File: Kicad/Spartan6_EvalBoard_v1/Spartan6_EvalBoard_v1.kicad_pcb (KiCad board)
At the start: 4 copper layers, 50 x 37.5 mm, 98 parts, among them J201 CON2X45, P301 PWR, P401 CONN_3X2, Q301 MOSFET_N, Q301 NPN, Q401 XC6SLX16, U301 XR21B1411, U401 24LC64T, U402 MX25L8006E, X301 USBMICRO, X401 XOSC

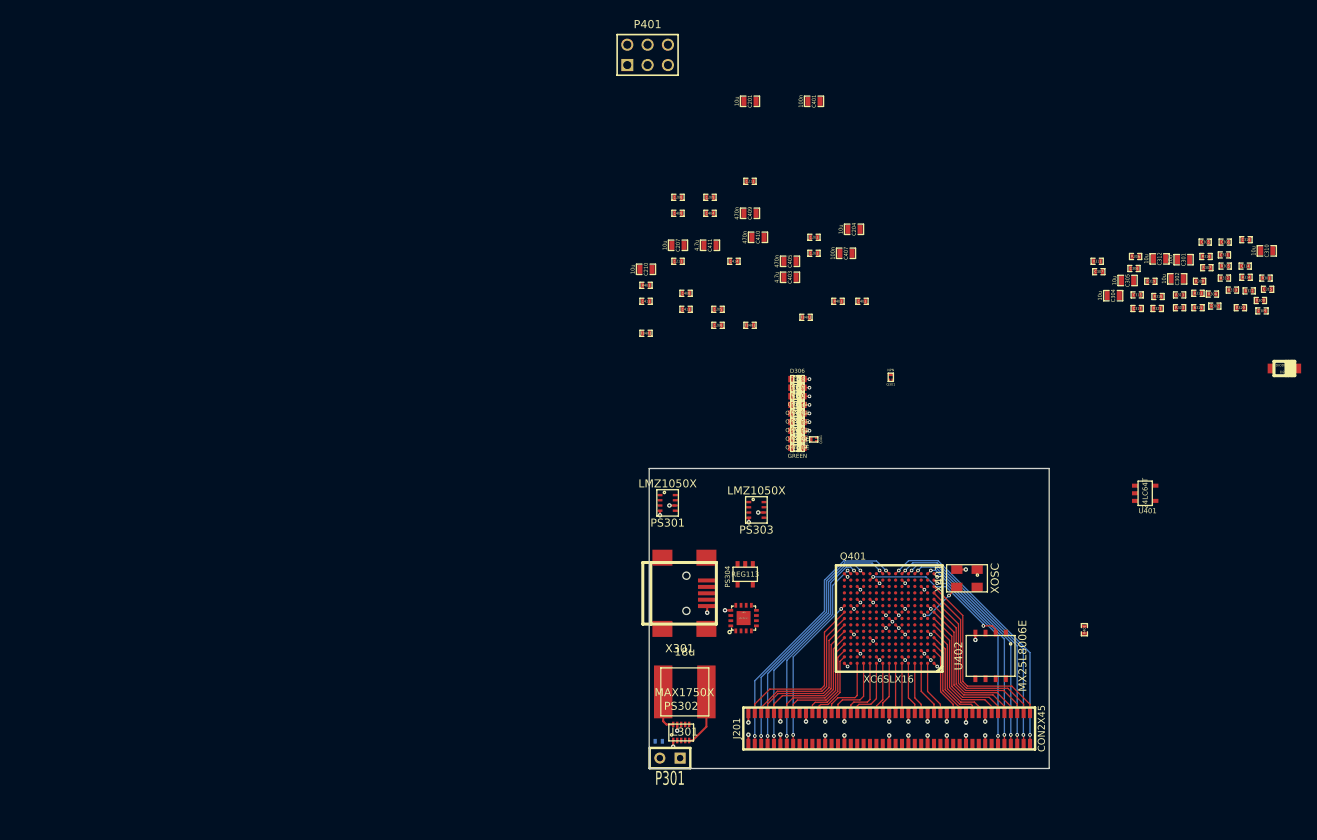
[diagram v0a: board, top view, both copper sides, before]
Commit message: BZR - Layout half done
Using LaunchPad Kicad
Layout more than half completed
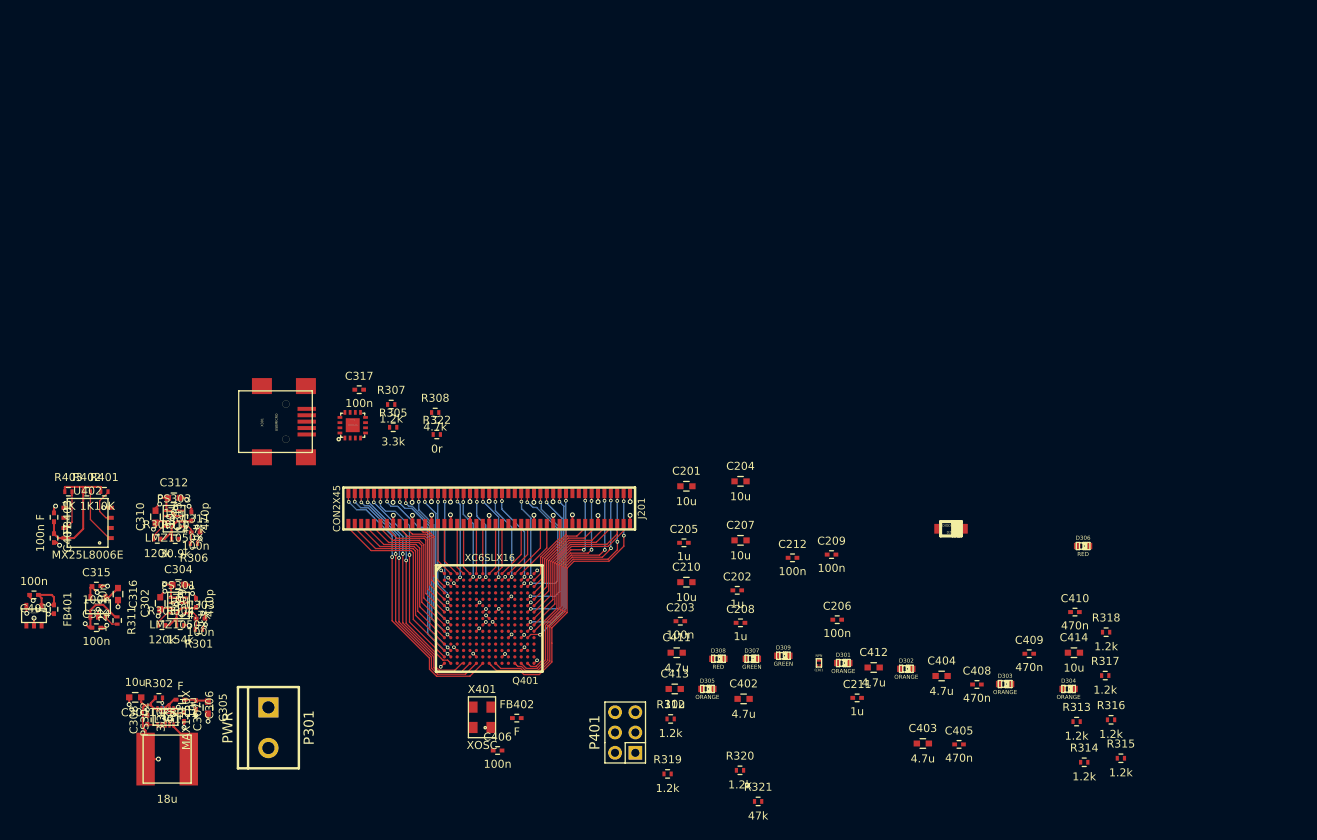
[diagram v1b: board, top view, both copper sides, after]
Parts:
- removed the Q301 at (130.2, 88.6)
- removed the Q301 at (120.6, 96.4)
- added Q301: NPN, Eric.mod:TSLP-3-1, F.Cu at (121.2, 124.3)
- C201, C204, C207, C210, C301, C302, C304, C305, C310, C312, C403, C411: footprint SM0603_Capa -> Capacitors_SMD.pretty:C_0603
- C202, C203, C205, C206, C208, C209, C211, C212, C303, C306, C307, C308, C309, C311, C313, C314, C315, C317, C406, C408: footprint SM0402_c -> Capacitors_SMD.pretty:C_0402
- C316, C402, C404, C412, C413, C414: footprint SM0402_c -> Capacitors_SMD.pretty:C_0603
- C401, C405, C407, C409, C410: footprint SM0603_Capa -> Capacitors_SMD.pretty:C_0402
- D201: footprint SOD-123FL -> Eric.mod:SOD-123FL
- D301, D302, D303, D304, D305, D306, D307, D308, D309: footprint LED-0603 -> LEDs.pretty:LED-0603
- FB301: footprint SM0402 -> Capacitors_SMD.pretty:C_0402; moved to F.Cu
- FB401, FB402, FB403: footprint SM0402 -> Capacitors_SMD.pretty:C_0402
- J201: footprint CON45X2 -> Eric.mod:CON45X2
- L301: footprint IND6x6 -> Eric.mod:IND6x6
- P301: footprint SIL-2 -> Connect.pretty:bornier2
- P401: footprint pin_array_3x2 -> Pin_Headers.pretty:Pin_Header_Straight_2x03
- PS301, PS303: footprint SIL08 -> Eric.mod:SIL08
- PS302: footprint TDFN10 -> Eric.mod:TDFN10
- PS304, U401: footprint SOT23-5 -> tinkerforge.mod:SOT23-5
- Q401: footprint CSG225 -> Eric.mod:CSG225
- R301, R302, R303, R304, R305, R306, R307, R308, R309, R310, R311, R312, R313, R314, R315, R316, R317, R318, R319, R320, R321, R322, R401, R402, R403: footprint SM0402_r -> Resistors_SMD.pretty:R_0402
- U301: footprint QFN-16 -> Eric.mod:QFN-16
- U402: footprint WSON8 -> Eric.mod:WSON8
- X301: footprint USB_MINI_B -> tinkerforge.mod:USB-MINI-B-SMD
- X401: footprint XTAL5032 -> Eric.mod:XTAL5032
- moved C315 151.0 mm to (30.9, 114.7)
- moved C314 150.5 mm to (30.9, 119.9)
- moved C316 147.8 mm to (33.6, 115.7), turned to 270 degrees
- moved C308 147.4 mm to (37.3, 131.4), turned to 90 degrees
- moved C310 142.8 mm to (38.3, 106.0), turned to 90 degrees
- moved C301 142.0 mm to (35.8, 128.6), turned to 180 degrees
- moved R302 140.8 mm to (38.7, 128.7)
- moved R301 140.4 mm to (43.7, 120.1), turned to 180 degrees
- moved U401 139.7 mm to (23.1, 118.4), turned to 0 degrees
- moved C309 138.2 mm to (43.3, 116.8), turned to 90 degrees
- moved R310 135.8 mm to (40.7, 108.8)
- moved R304 135.5 mm to (41.4, 119.6)
- moved R309 134.2 mm to (38.5, 108.8)
- moved C303 134.1 mm to (43.9, 118.8)
- moved C302 133.4 mm to (38.9, 116.8), turned to 90 degrees
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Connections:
- J201 pad 14: (no net) -> /IO Connector/IO14
- J201 pad 18: (no net) -> /IO Connector/IO18
- J201 pad 20: (no net) -> /IO Connector/IO20
- J201 pad 24: (no net) -> /IO Connector/IO24
- J201 pad 26: (no net) -> /IO Connector/IO26
- J201 pad 30: (no net) -> /IO Connector/IO30
- J201 pad 32: (no net) -> /IO Connector/IO32
- J201 pad 36: (no net) -> /IO Connector/IO36
- J201 pad 38: (no net) -> /IO Connector/IO38
- J201 pad 42: (no net) -> /IO Connector/IO42
- J201 pad 44: (no net) -> /IO Connector/IO44
- J201 pad 48: (no net) -> /IO Connector/IO48
- J201 pad 50: (no net) -> /IO Connector/IO50
- J201 pad 56: (no net) -> /IO Connector/IO56
- J201 pad 58: (no net) -> /IO Connector/IO58
- J201 pad 62: (no net) -> /IO Connector/IO62
- J201 pad 64: (no net) -> /IO Connector/IO64
- J201 pad 68: (no net) -> /IO Connector/IO68
- J201 pad 70: (no net) -> /IO Connector/IO70
- PS302 pad 7: (no net) -> Net-(PS302-Pad7)
- Q401 pad B11: (no net) -> /IO Connector/IO48
- Q401 pad B13: (no net) -> /IO Connector/IO50
- Q401 pad B14: (no net) -> /IO Connector/IO56
- Q401 pad B3: (no net) -> /IO Connector/IO36
- Q401 pad B5: (no net) -> /IO Connector/IO38
- Q401 pad B7: (no net) -> /IO Connector/IO42
- Q401 pad B9: (no net) -> /IO Connector/IO44
- Q401 pad C10: (no net) -> Net-(Q401-PadC10)
- Q401 pad C11: (no net) -> Net-(Q401-PadC11)
- Q401 pad C12: (no net) -> Net-(Q401-PadC12)
- Q401 pad C14: (no net) -> /IO Connector/IO58
- Q401 pad C2: (no net) -> /IO Connector/IO32
- Q401 pad C4: (no net) -> Net-(Q401-PadC4)
- Q401 pad C5: (no net) -> Net-(Q401-PadC5)
- Q401 pad C6: (no net) -> Net-(Q401-PadC6)
- Q401 pad C7: (no net) -> Net-(Q401-PadC7)
- Q401 pad C8: (no net) -> Net-(Q401-PadC8)
- Q401 pad C9: (no net) -> Net-(Q401-PadC9)
- Q401 pad D10: (no net) -> Net-(Q401-PadD10)
- Q401 pad D11: (no net) -> Net-(Q401-PadD11)
- Q401 pad D13: (no net) -> Net-(Q401-PadD13)
- Q401 pad D3: (no net) -> Net-(Q401-PadD3)
- Q401 pad D4: (no net) -> Net-(Q401-PadD4)
- Q401 pad D5: (no net) -> Net-(Q401-PadD5)
- Q401 pad D6: (no net) -> Net-(Q401-PadD6)
- Q401 pad D7: (no net) -> Net-(Q401-PadD7)
- Q401 pad D8: (no net) -> Net-(Q401-PadD8)
- Q401 pad E14: (no net) -> /IO Connector/IO62
- Q401 pad E2: (no net) -> /IO Connector/IO30
- Q401 pad E3: (no net) -> Net-(Q401-PadE3)
- Q401 pad E4: (no net) -> Net-(Q401-PadE4)
- Q401 pad E5: (no net) -> Net-(Q401-PadE5)
- Q401 pad E6: (no net) -> Net-(Q401-PadE6)
- Q401 pad E7: (no net) -> Net-(Q401-PadE7)
- Q401 pad E8: (no net) -> Net-(Q401-PadE8)
- Q401 pad E9: (no net) -> Net-(Q401-PadE9)
- Q401 pad F10: (no net) -> Net-(Q401-PadF10)
- Q401 pad F11: (no net) -> Net-(Q401-PadF11)
- Q401 pad F12: (no net) -> Net-(Q401-PadF12)
- Q401 pad F13: (no net) -> Net-(Q401-PadF13)
- Q401 pad F3: (no net) -> Net-(Q401-PadF3)
- Q401 pad F4: (no net) -> Net-(Q401-PadF4)
- Q401 pad F5: (no net) -> Net-(Q401-PadF5)
- Q401 pad F8: (no net) -> Net-(Q401-PadF8)
- Q401 pad G11: (no net) -> Net-(Q401-PadG11)
- Q401 pad G12: (no net) -> Net-(Q401-PadG12)
- Q401 pad G13: (no net) -> Net-(Q401-PadG13)
- Q401 pad G14: (no net) -> /IO Connector/IO64
- Q401 pad G2: (no net) -> /IO Connector/IO26
- Q401 pad G3: (no net) -> Net-(Q401-PadG3)
- Q401 pad G5: (no net) -> Net-(Q401-PadG5)
- Q401 pad H10: (no net) -> Net-(Q401-PadH10)
- Q401 pad H11: (no net) -> Net-(Q401-PadH11)
- Q401 pad H12: (no net) -> Net-(Q401-PadH12)
- Q401 pad H13: (no net) -> Net-(Q401-PadH13)
- Q401 pad H3: (no net) -> Net-(Q401-PadH3)
- Q401 pad H4: (no net) -> Net-(Q401-PadH4)
- Q401 pad H5: (no net) -> Net-(Q401-PadH5)
- Q401 pad H6: (no net) -> Net-(Q401-PadH6)
- Q401 pad H7: 1.2V -> (no net)
- Q401 pad J11: (no net) -> Net-(Q401-PadJ11)
- Q401 pad J13: (no net) -> Net-(Q401-PadJ13)
- Q401 pad J14: (no net) -> /IO Connector/IO68
- Q401 pad J2: (no net) -> /IO Connector/IO24
- Q401 pad J4: (no net) -> Net-(Q401-PadJ4)
- Q401 pad J5: (no net) -> Net-(Q401-PadJ5)
- Q401 pad K10: (no net) -> Net-(Q401-PadK10)
- Q401 pad K11: (no net) -> Net-(Q401-PadK11)
- Q401 pad K12: (no net) -> Net-(Q401-PadK12)
- Q401 pad K13: (no net) -> Net-(Q401-PadK13)
- Q401 pad K3: (no net) -> Net-(Q401-PadK3)
- Q401 pad K4: (no net) -> Net-(Q401-PadK4)
- Q401 pad K5: (no net) -> Net-(Q401-PadK5)
- Q401 pad K8: (no net) -> Net-(Q401-PadK8)
- Q401 pad L10: (no net) -> Net-(Q401-PadL10)
- Q401 pad L12: (no net) -> Net-(Q401-PadL12)
- Q401 pad L14: (no net) -> /IO Connector/IO70
- Q401 pad L2: (no net) -> /IO Connector/IO20
- Q401 pad L3: (no net) -> Net-(Q401-PadL3)
- Q401 pad L5: (no net) -> Net-(Q401-PadL5)
- Q401 pad L6: (no net) -> Net-(Q401-PadL6)
- Q401 pad L7: (no net) -> Net-(Q401-PadL7)
- Q401 pad L8: (no net) -> Net-(Q401-PadL8)
- Q401 pad M11: (no net) -> Net-(Q401-PadM11)
- Q401 pad M13: (no net) -> Net-(Q401-PadM13)
- Q401 pad M3: (no net) -> Net-(Q401-PadM3)
- Q401 pad M4: (no net) -> Net-(Q401-PadM4)
- Q401 pad M5: (no net) -> Net-(Q401-PadM5)
- Q401 pad M6: (no net) -> Net-(Q401-PadM6)
- Q401 pad M8: (no net) -> Net-(Q401-PadM8)
- Q401 pad N2: (no net) -> /IO Connector/IO18
- Q401 pad N4: (no net) -> Net-(Q401-PadN4)
- Q401 pad N5: (no net) -> Net-(Q401-PadN5)
- Q401 pad N6: (no net) -> Net-(Q401-PadN6)
- Q401 pad N7: (no net) -> Net-(Q401-PadN7)
- Q401 pad N8: (no net) -> Net-(Q401-PadN8)
- Q401 pad P13: (no net) -> Net-(Q401-PadP13)
- Q401 pad P2: (no net) -> /IO Connector/IO14
- Q401 pad P3: (no net) -> Net-(Q401-PadP3)
- Q401 pad P5: (no net) -> Net-(Q401-PadP5)
- Q401 pad P7: (no net) -> Net-(Q401-PadP7)
- U301 pad 2: (no net) -> Net-(U301-Pad2)
- X301 pad 4: (no net) -> Net-(X301-Pad4)
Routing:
- net /IO Connector/IO14: track 0.00 -> 25.0 mm, vias 0 -> 2
- net /IO Connector/IO18: track 0.00 -> 22.9 mm, vias 0 -> 2
- net /IO Connector/IO70: track 0.00 -> 20.8 mm, vias 0 -> 2
- net /IO Connector/IO20: track 0.00 -> 20.7 mm, vias 0 -> 2
- net /IO Connector/IO68: track 0.00 -> 20.1 mm, vias 0 -> 2
- net /IO Connector/IO64: track 0.00 -> 19.6 mm, vias 0 -> 2
- net /SPARTAN6/FLASH_MISO: track 19.2 -> 0.00 mm, vias 2 -> 0
- net /IO Connector/IO24: track 0.00 -> 18.2 mm, vias 0 -> 2
- net /IO Connector/IO62: track 0.00 -> 17.8 mm, vias 0 -> 2
- net Net-(C407-Pad1): track 0.00 -> 17.1 mm
- net /IO Connector/IO58: track 0.00 -> 17.0 mm, vias 0 -> 2
- net /IO Connector/IO26: track 0.00 -> 16.3 mm, vias 0 -> 2
- net /IO Connector/IO30: track 0.00 -> 14.0 mm, vias 0 -> 2
- net /IO Connector/IO50: track 0.00 -> 12.3 mm, vias 0 -> 2
- net GND: track 52.0 -> 64.1 mm, vias 65 -> 77
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- removed copper zone on Inner2.Cu, net GND
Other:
- board outline removed
- net class Ground added: clearance 0.127, trace_width 0.254, via_dia 0.6096, via_drill 0.3556
- net class Power: via_dia 0.5588 -> 0.6096; via_drill 0.3048 -> 0.3556

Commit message: Layout completed, just need to run DRC.
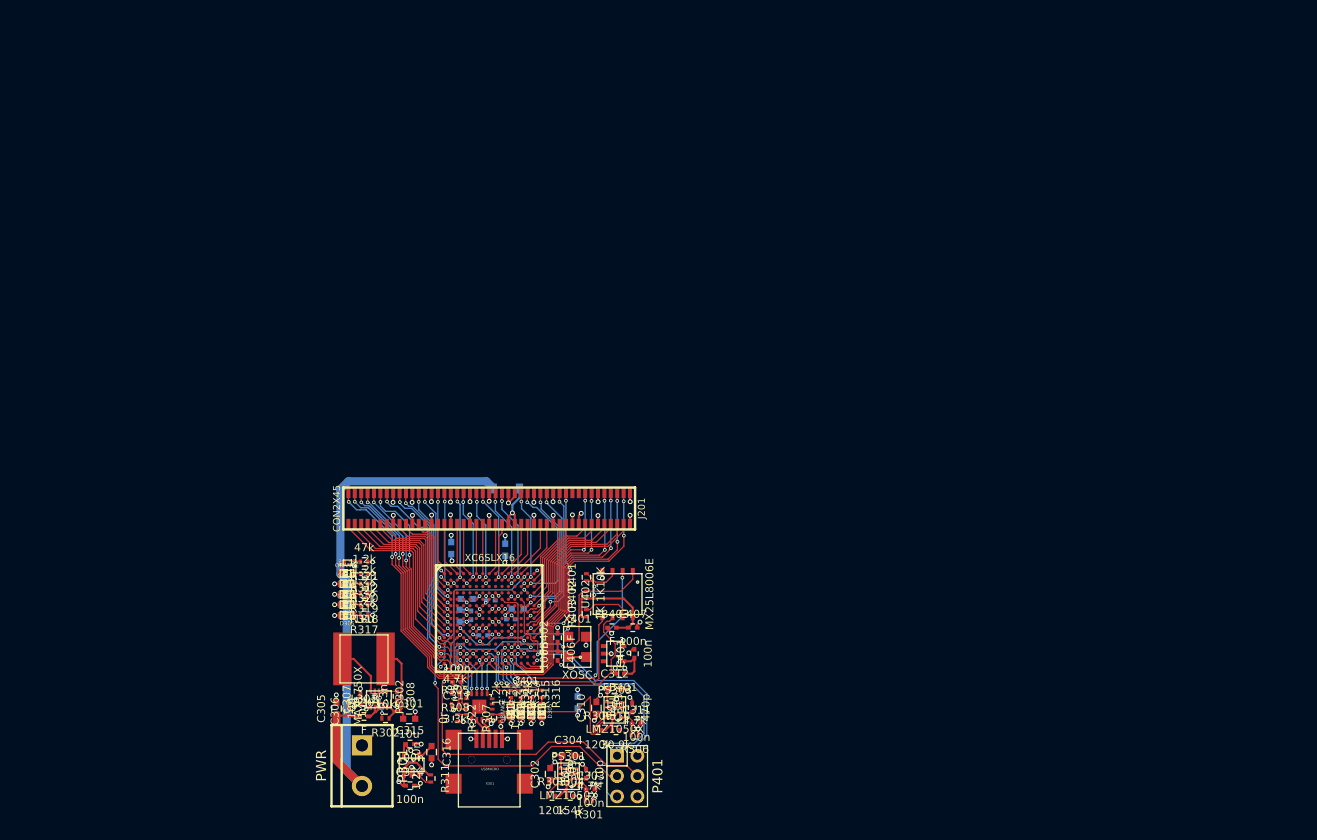
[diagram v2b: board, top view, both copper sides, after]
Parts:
- removed C201, C204, C207, C210: 10u, Capacitors_SMD.pretty:C_0603
- removed C202, C205, C208, C211: 1u, Capacitors_SMD.pretty:C_0402
- removed C203, C206, C209, C212: 100n, Capacitors_SMD.pretty:C_0402
- removed C404: 4.7u, Capacitors_SMD.pretty:C_0603
- C402, C403, C405, C408, C409, C410, C411, C412, C413, C414, D201: moved to B.Cu
- moved R317 92.9 mm to (64.4, 118.4), turned to 180 degrees
- moved R318 92.8 mm to (64.4, 117.0), turned to 180 degrees
- moved D306 92.4 mm to (62.2, 118.4), turned to 180 degrees
- moved C410 75.5 mm to (77.8, 118.3), turned to 90 degrees
- moved C401 75.4 mm to (98.2, 123.2), turned to 90 degrees
- moved R315 74.1 mm to (85.2, 128.2), turned to 270 degrees
- moved C407 73.2 mm to (98.0, 119.9), turned to 0 degrees
- moved U401 72.6 mm to (95.5, 123.2), turned to 270 degrees
- moved C414 72.3 mm to (82.0, 110.2), turned to 90 degrees
- moved R316 71.2 mm to (86.6, 128.2), turned to 270 degrees
- moved FB401 71.2 mm to (96.3, 125.7), turned to 180 degrees
- moved FB403 71.1 mm to (95.3, 119.9), turned to 0 degrees
- moved R314 70.9 mm to (84.0, 128.2), turned to 270 degrees
- moved R313 70.8 mm to (82.7, 128.2), turned to 270 degrees
- moved C409 67.6 mm to (80.2, 116.5)
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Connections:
- FB402 pad 1: 3.3V -> Net-(C406-Pad1)
- FB402 pad 2: Net-(C406-Pad1) -> 3.3V
- PS302 pad 7: Net-(PS302-Pad7) -> (no net)
- Q401 pad C10: Net-(Q401-PadC10) -> (no net)
- Q401 pad C11: Net-(Q401-PadC11) -> (no net)
- Q401 pad C12: Net-(Q401-PadC12) -> (no net)
- Q401 pad C4: Net-(Q401-PadC4) -> (no net)
- Q401 pad C5: Net-(Q401-PadC5) -> (no net)
- Q401 pad C6: Net-(Q401-PadC6) -> (no net)
- Q401 pad C7: Net-(Q401-PadC7) -> (no net)
- Q401 pad C8: Net-(Q401-PadC8) -> (no net)
- Q401 pad C9: Net-(Q401-PadC9) -> (no net)
- Q401 pad D10: Net-(Q401-PadD10) -> (no net)
- Q401 pad D11: Net-(Q401-PadD11) -> (no net)
- Q401 pad D13: Net-(Q401-PadD13) -> (no net)
- Q401 pad D3: Net-(Q401-PadD3) -> (no net)
- Q401 pad D4: Net-(Q401-PadD4) -> (no net)
- Q401 pad D5: Net-(Q401-PadD5) -> (no net)
- Q401 pad D6: Net-(Q401-PadD6) -> (no net)
- Q401 pad D7: Net-(Q401-PadD7) -> (no net)
- Q401 pad D8: Net-(Q401-PadD8) -> (no net)
- Q401 pad E3: Net-(Q401-PadE3) -> (no net)
- Q401 pad E4: Net-(Q401-PadE4) -> (no net)
- Q401 pad E5: Net-(Q401-PadE5) -> (no net)
- Q401 pad E6: Net-(Q401-PadE6) -> (no net)
- Q401 pad E7: Net-(Q401-PadE7) -> (no net)
- Q401 pad E8: Net-(Q401-PadE8) -> (no net)
- Q401 pad E9: Net-(Q401-PadE9) -> (no net)
- Q401 pad F10: Net-(Q401-PadF10) -> (no net)
- Q401 pad F11: Net-(Q401-PadF11) -> (no net)
- Q401 pad F12: Net-(Q401-PadF12) -> (no net)
- Q401 pad F13: Net-(Q401-PadF13) -> (no net)
- Q401 pad F3: Net-(Q401-PadF3) -> (no net)
- Q401 pad F4: Net-(Q401-PadF4) -> (no net)
- Q401 pad F5: Net-(Q401-PadF5) -> (no net)
- Q401 pad F8: Net-(Q401-PadF8) -> (no net)
- Q401 pad G11: Net-(Q401-PadG11) -> (no net)
- Q401 pad G12: Net-(Q401-PadG12) -> (no net)
- Q401 pad G13: Net-(Q401-PadG13) -> (no net)
- Q401 pad G3: Net-(Q401-PadG3) -> (no net)
- Q401 pad G5: Net-(Q401-PadG5) -> (no net)
- Q401 pad H10: Net-(Q401-PadH10) -> (no net)
- Q401 pad H11: Net-(Q401-PadH11) -> (no net)
- Q401 pad H12: Net-(Q401-PadH12) -> (no net)
- Q401 pad H13: Net-(Q401-PadH13) -> (no net)
- Q401 pad H3: Net-(Q401-PadH3) -> (no net)
- Q401 pad H4: Net-(Q401-PadH4) -> (no net)
- Q401 pad H5: Net-(Q401-PadH5) -> (no net)
- Q401 pad H6: Net-(Q401-PadH6) -> (no net)
- Q401 pad J11: Net-(Q401-PadJ11) -> (no net)
- Q401 pad J13: Net-(Q401-PadJ13) -> (no net)
- Q401 pad J4: Net-(Q401-PadJ4) -> (no net)
- Q401 pad J5: Net-(Q401-PadJ5) -> (no net)
- Q401 pad K10: Net-(Q401-PadK10) -> (no net)
- Q401 pad K11: Net-(Q401-PadK11) -> (no net)
- Q401 pad K12: Net-(Q401-PadK12) -> (no net)
- Q401 pad K13: Net-(Q401-PadK13) -> (no net)
- Q401 pad K3: Net-(Q401-PadK3) -> (no net)
- Q401 pad K4: Net-(Q401-PadK4) -> (no net)
- Q401 pad K5: Net-(Q401-PadK5) -> (no net)
- Q401 pad K8: Net-(Q401-PadK8) -> (no net)
- Q401 pad L10: Net-(Q401-PadL10) -> (no net)
- Q401 pad L12: Net-(Q401-PadL12) -> (no net)
- Q401 pad L14: /IO Connector/IO70 -> (no net)
- Q401 pad L15: /SPARTAN6/I2C_EE_SCL -> /IO Connector/IO70
- Q401 pad L3: Net-(Q401-PadL3) -> /POWER/PC_RX
- Q401 pad L5: Net-(Q401-PadL5) -> (no net)
- Q401 pad L6: Net-(Q401-PadL6) -> (no net)
- Q401 pad L7: Net-(Q401-PadL7) -> (no net)
- Q401 pad L8: Net-(Q401-PadL8) -> (no net)
- Q401 pad L9: /POWER/PC_GPIO1 -> (no net)
- Q401 pad M10: /POWER/PC_GPIO2 -> (no net)
- Q401 pad M11: Net-(Q401-PadM11) -> (no net)
- Q401 pad M13: Net-(Q401-PadM13) -> (no net)
- Q401 pad M3: Net-(Q401-PadM3) -> /POWER/PC_TX
- Q401 pad M4: Net-(Q401-PadM4) -> (no net)
- Q401 pad M5: Net-(Q401-PadM5) -> (no net)
- Q401 pad M6: Net-(Q401-PadM6) -> (no net)
- Q401 pad M8: Net-(Q401-PadM8) -> (no net)
- Q401 pad M9: /POWER/PC_GPIO3 -> (no net)
- Q401 pad N10: /POWER/PC_RX -> /POWER/LED3
- Q401 pad N11: /POWER/PC_TX -> (no net)
- Q401 pad N14: /POWER/LED1 -> /SPARTAN6/I2C_EE_SCL
- Q401 pad N15: /POWER/LED2 -> (no net)
- Q401 pad N4: Net-(Q401-PadN4) -> (no net)
- Q401 pad N5: Net-(Q401-PadN5) -> (no net)
- Q401 pad N6: Net-(Q401-PadN6) -> (no net)
- Q401 pad N7: Net-(Q401-PadN7) -> (no net)
- Q401 pad N8: Net-(Q401-PadN8) -> /POWER/LED1
- Q401 pad N9: /POWER/PC_GPIO4 -> /POWER/LED2
- Q401 pad P13: Net-(Q401-PadP13) -> (no net)
- Q401 pad P14: /POWER/LED3 -> (no net)
- Q401 pad P15: /POWER/LED4 -> (no net)
- Q401 pad P3: Net-(Q401-PadP3) -> /POWER/PC_GPIO0
- Q401 pad P5: Net-(Q401-PadP5) -> /POWER/PC_GPIO1
- Q401 pad P7: Net-(Q401-PadP7) -> /POWER/PC_GPIO2
- Q401 pad P9: /POWER/PC_GPIO5 -> /POWER/PC_GPIO3
- Q401 pad R10: /POWER/PC_GPIO0 -> /POWER/LED4
- U301 pad 2: Net-(U301-Pad2) -> (no net)
- U301 pad 3: /POWER/PC_GPIO5 -> (no net)
- U301 pad 4: /POWER/PC_GPIO4 -> (no net)
- X301 pad 4: Net-(X301-Pad4) -> (no net)
- X401 pad 4: 3.3V -> Net-(C406-Pad1)
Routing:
- net 1.2V: track 5.30 -> 106.7 mm, vias 1 -> 9
- net VCC: track 2.98 -> 74.1 mm
- net /SPARTAN6/TCK: track 0.00 -> 57.5 mm, vias 0 -> 2
- net /SPARTAN6/TDO: track 0.00 -> 55.6 mm, vias 0 -> 2
- net 5V: track 19.0 -> 61.8 mm, vias 5 -> 7
- net /SPARTAN6/TMS: track 0.00 -> 40.9 mm, vias 0 -> 1
- net /SPARTAN6/TDI: track 0.00 -> 36.7 mm, vias 0 -> 1
- net /SPARTAN6/FLASH_CSn: track 6.94 -> 34.6 mm, vias 0 -> 2
- net /SPARTAN6/FLASH_MISO: track 0.00 -> 27.5 mm, vias 0 -> 4
- net /POWER/5V_USB: track 7.57 -> 32.3 mm, vias 1 -> 5
- net /SPARTAN6/FLASH_SCK: track 0.00 -> 24.1 mm, vias 0 -> 2
- net GND: track 64.1 -> 87.1 mm, vias 77 -> 97
- net /SPARTAN6/FLASH_MOSI: track 0.00 -> 22.2 mm, vias 0 -> 2
- net 3.3V: track 6.53 -> 28.1 mm, vias 3 -> 36
- net /SPARTAN6/CLK: track 0.00 -> 16.7 mm, vias 0 -> 2
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- added copper zone on L3, net 3.3V
- added copper zone on L3, net 5V
- added copper zone on L2, net GND
